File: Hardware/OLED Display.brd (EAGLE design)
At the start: 50 x 15 mm, 23 parts, among them J1 SM04B-SRSS-TB, J2 SM04B-SRSS-TB, U1 QG-2832TLBFG02, U2 APX803

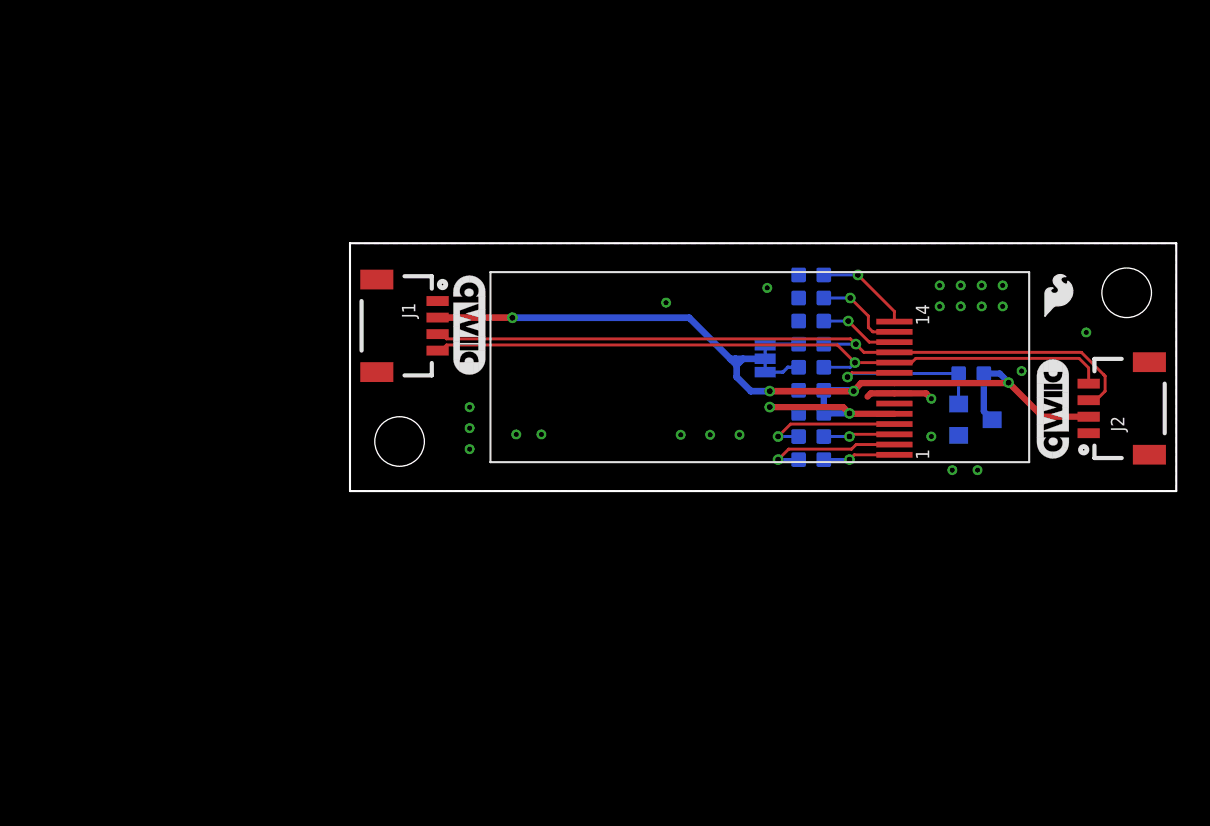
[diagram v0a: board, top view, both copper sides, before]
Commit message: Replaces parts not in the SparkFun Eagle Libraries, adds logos, moves qwiic connectors and standoffs
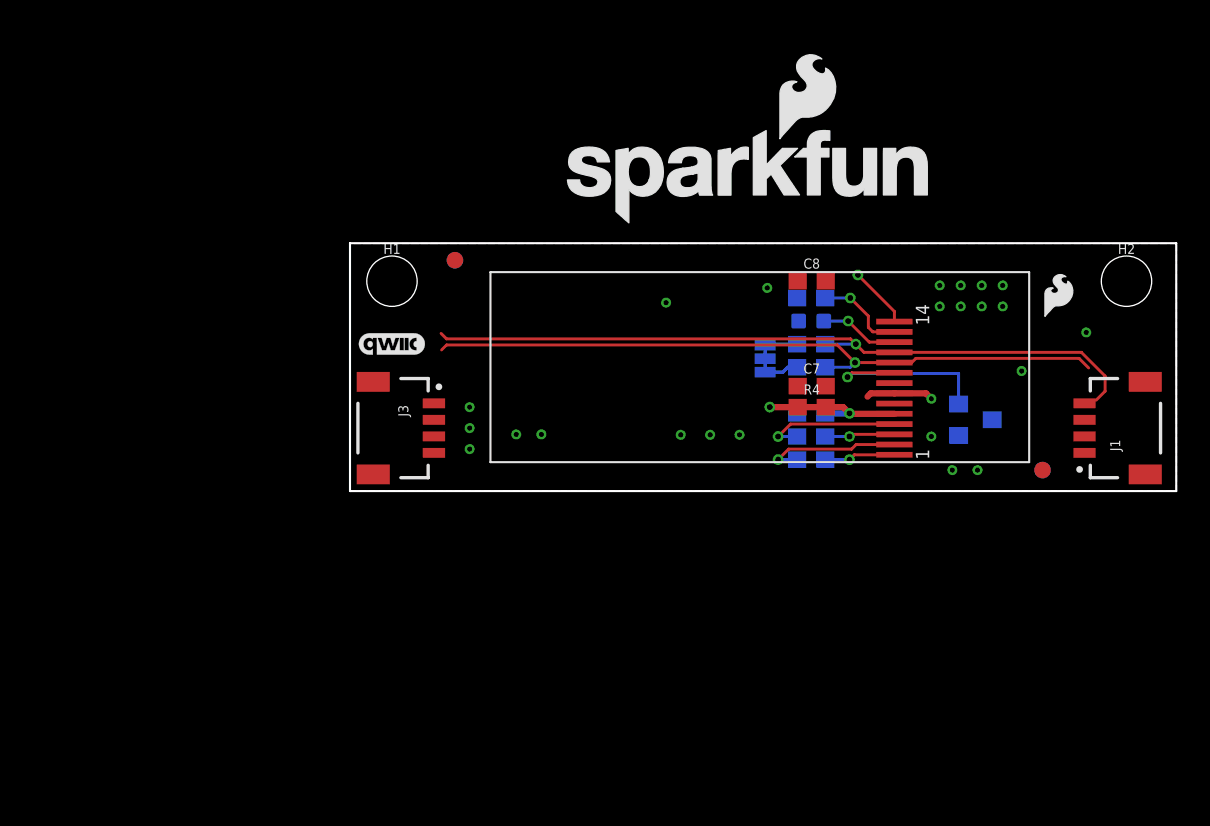
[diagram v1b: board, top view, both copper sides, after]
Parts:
- removed C3: 4.7uF ±10% 6.3V, Discrete:0603
- removed C6: 4.7uF ±10% 16V, Discrete:0603
- removed J2: SM04B-SRSS-TB, Connector:JST-SH-4P
- removed U$11, U$12: (no value), SparkFun-Aesthetics_Font_Logo:QWIIC_6MM
- removed U$6: (no value), Z_silkscreen_package:QWIIC-LOGO-MEDIUM
- added C7, C8: 4.7uF, SparkFun-Capacitors:0603
- added FD1, FD2, FD3, FD4: FIDUCIAL1X2, SparkFun-Aesthetics:FIDUCIAL-1X2
- added FRAME2: FRAME-LETTER, SparkFun-Aesthetics:CREATIVE_COMMONS
- added H1, H2: STAND-OFFTIGHT, SparkFun-Hardware:STAND-OFF-TIGHT
- added J3: QWIIC_RIGHT_ANGLE, SparkFun-Connectors:JST04_1MM_RA
- added LOGO1: SFE_LOGO_NAME_FLAME.2_INCH, SparkFun-Aesthetics:SFE_LOGO_NAME_FLAME_.2
- added LOGO3: QWIIC_LOGO_4MM, SparkFun-Aesthetics:QWIIC_4MM
- added LOGO4: SPECIAL_INSTRUCTIONS-ORDERING, SparkFun-Aesthetics:ORDERING_INSTRUCTIONS
- C1, C2: value 1uF ±10% 16V -> 1.0uF; device Discrete:0603 -> SparkFun-Capacitors:0603
- C4: value 0.1uF ±10% 25V -> 0.1uF; device Discrete:0603 -> SparkFun-Capacitors:0603
- C5: value 2.2uF ±10% 16V -> 2.2uF; device Discrete:0603 -> SparkFun-Capacitors:0603
- J1: value SM04B-SRSS-TB -> QWIIC_RIGHT_ANGLE; device Connector:JST-SH-4P -> SparkFun-Connectors:JST04_1MM_RA
- R1, R2, R4: value 10K ±5% -> 10k; device Discrete:0603 -> SparkFun-Resistors:0603
- moved J1 39.6 mm to (44.5, 3.81)
- moved R4 9.86 mm to (27.9, 5.08), flipped to the top, turned to 0 degrees
- renumbered JP1 to I2C
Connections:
- net OLED_RST# renamed RST
- removed net +3V3: C3.1, C4.1, I2C.2, J1.2, J2.2, R4.2, U1.5, U1.8, U2.3
- new net 3.3V: C4.1, C8.2, I2C.2, J1.2, J3.2, R4.2, U1.5, U1.8, U2.3
- net GND: now also C7.1, C8.1, J3.1; no longer C3.2, C6.2, J1.NC1, J1.NC2, J2.1, J2.NC1, J2.NC2
- net N$7: now also C7.2; no longer C6.1
- net SCL: now also J3.4; no longer J2.4
- net SDA: now also J3.3; no longer J2.3
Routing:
- net +3V3: track 63.0 -> 0.00 mm, vias 6 -> 0
- net 3.3V: track 0.00 -> 9.18 mm, vias 0 -> 2
- net N$7: track 5.81 -> 3.74 mm
- net SCL: track 43.3 -> 42.0 mm
- net SDA: track 45.5 -> 44.8 mm

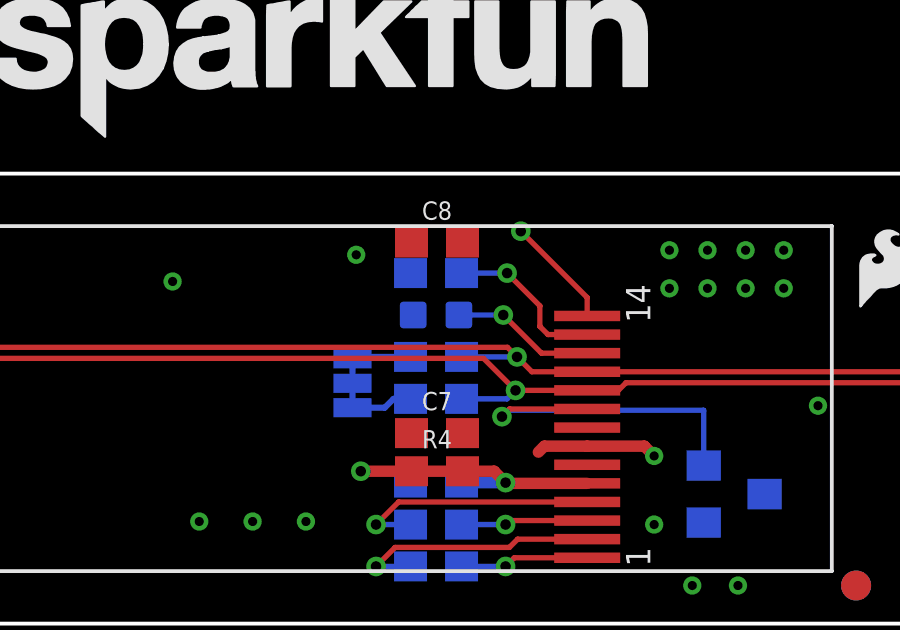
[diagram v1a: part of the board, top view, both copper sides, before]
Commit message: Replaces more parts
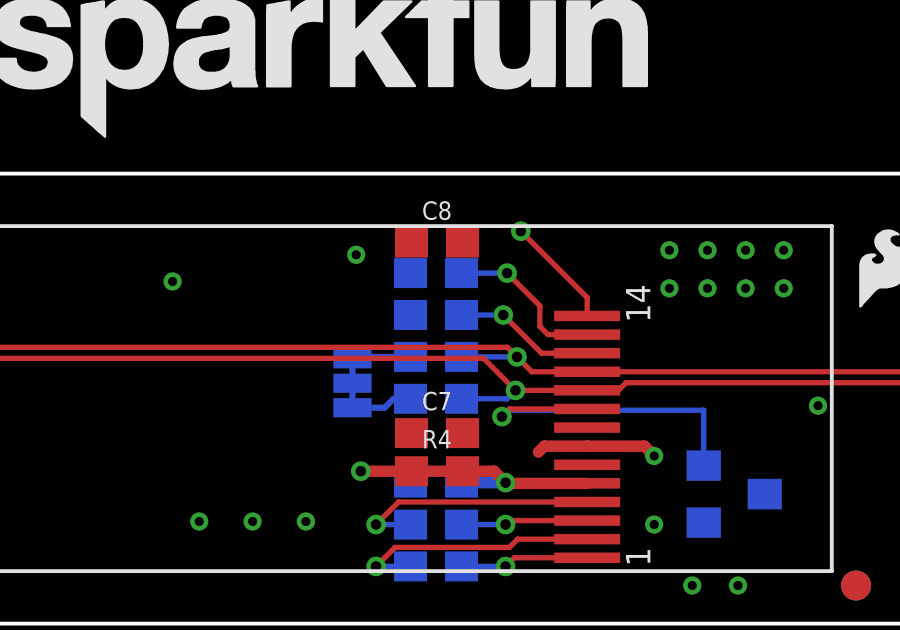
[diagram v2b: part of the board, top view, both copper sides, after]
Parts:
- R3: value 560K 10% -> 470k; device Discrete:0603 -> SparkFun-Resistors:0603
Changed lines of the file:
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@@
 <attribute name="VALUE" value="10k" x="29.305" y="7.4549" size="0.635" layer="28" ratio="10" rot="MR0"/>
 </element>
-<element name="R3" library="Discrete" package="0603" value="560K 10%" x="27.908" y="10.287" smashed="yes" rot="MR180">
+<element name="R3" library="SparkFun-Resistors" package="0603" value="470k" x="27.908" y="10.287" smashed="yes" rot="MR180">
 <attribute name="NAME" x="27.273" y="10.668" size="0.8128" layer="26" ratio="10" rot="MR180"/>
 <attribute name="NAME" x="26.638" y="10.541" size="0.635" layer="34" ratio="10" rot="MR180"/>
-<attribute name="VALUE" x="26.511" y="11.7221" size="0.635" layer="28" ratio="10" rot="MR180"/>
+<attribute name="PROD_ID" value="RES-16181" x="27.908" y="10.287" size="1.778" layer="28" rot="MR180" display="off"/>
+<attribute name="VALUE" value="470k" x="26.511" y="11.7221" size="0.635" layer="28" ratio="10" rot="MR180"/>
 </element>
 <element name="U1" library="Module" package="OLED-12832" value="QG-2832TLBFG02" x="8.5" y="1.75" smashed="yes"/>
@@
 <wire x1="31.4218" y1="9.015" x2="30.1498" y2="10.287" width="0.1778" layer="1"/>
 <via x="30.1498" y="10.287" extent="1-16" drill="0.35"/>
-<wire x1="28.67" y1="10.287" x2="30.1498" y2="10.287" width="0.1778" layer="16"/>
+<wire x1="28.758" y1="10.287" x2="30.1498" y2="10.287" width="0.1778" layer="16"/>
 </signal>
 <signal name="GND">
-<contactref element="U1" pad="7"/>
 <polygon width="0.1778" layer="1">
 <vertex x="0" y="0"/>
@@
 <vertex x="0" y="14.986"/>
 </polygon>
-<via x="35.179" y="5.588" extent="1-16" drill="0.3048"/>
-<wire x1="32.945" y1="5.915" x2="34.852" y2="5.915" width="0.381" layer="1"/>
-<wire x1="34.852" y1="5.915" x2="35.179" y2="5.588" width="0.381" layer="1"/>
-<wire x1="32.945" y1="5.915" x2="31.5182" y2="5.915" width="0.381" layer="1"/>
-<wire x1="31.5182" y1="5.915" x2="31.3182" y2="5.715" width="0.381" layer="1"/>
 <via x="35.179" y="3.302" extent="1-16" drill="0.3048"/>
 <via x="40.64" y="7.2644" extent="1-16" drill="0.3048"/>
@@
 <contactref element="J3" pad="1"/>
 <contactref element="U2" pad="1"/>
-<wire x1="5.08" y1="5.31" x2="44.45" y2="2.31" width="0" layer="19" extent="1-1"/>
-<wire x1="27.09" y1="12.7" x2="5.08" y2="5.31" width="0" layer="19" extent="1-1"/>
-<wire x1="27.09" y1="6.35" x2="27.09" y2="12.7" width="0" layer="19" extent="1-1"/>
-<wire x1="7.239" y1="2.54" x2="27.09" y2="6.35" width="0" layer="19" extent="1-1"/>
-<wire x1="7.239" y1="3.81" x2="7.239" y2="2.54" width="0" layer="19" extent="1-1"/>
-<wire x1="7.239" y1="5.08" x2="7.239" y2="3.81" width="0" layer="19" extent="1-1"/>
-<wire x1="10.0584" y1="3.429" x2="7.239" y2="3.81" width="0" layer="19" extent="1-1"/>
-<wire x1="11.5824" y1="3.429" x2="10.0584" y2="3.429" width="0" layer="19" extent="1-1"/>
-<wire x1="20.0152" y1="3.4036" x2="11.5824" y2="3.429" width="0" layer="19" extent="1-1"/>
-<wire x1="21.7932" y1="3.4036" x2="20.0152" y2="3.4036" width="0" layer="19" extent="1-1"/>
-<wire x1="23.5712" y1="3.4036" x2="21.7932" y2="3.4036" width="0" layer="19" extent="1-1"/>
-<wire x1="27.058" y1="4.699" x2="23.5712" y2="3.4036" width="0" layer="19" extent="16-16"/>
-<wire x1="31.3182" y1="5.715" x2="27.058" y2="4.699" width="0" layer="19" extent="1-16"/>
-<wire x1="35.179" y1="3.302" x2="35.179" y2="5.588" width="0" layer="19" extent="1-1"/>
-<wire x1="36.83" y1="3.368" x2="35.179" y2="3.302" width="0" layer="19" extent="16-16"/>
-<wire x1="36.449" y1="1.27" x2="36.83" y2="3.368" width="0" layer="19" extent="16-16"/>
-<wire x1="37.973" y1="1.27" x2="36.449" y2="1.27" width="0" layer="19" extent="1-1"/>
-<wire x1="40.64" y1="7.2644" x2="36.83" y2="3.368" width="0" layer="19" extent="16-16"/>
+<contactref element="U1" pad="7"/>
+<via x="35.179" y="5.588" extent="1-16" drill="0.3048"/>
+<wire x1="32.945" y1="5.915" x2="34.852" y2="5.915" width="0.381" layer="1"/>
+<wire x1="34.852" y1="5.915" x2="35.179" y2="5.588" width="0.381" layer="1"/>
+<wire x1="32.945" y1="5.915" x2="31.5182" y2="5.915" width="0.381" layer="1"/>
+<wire x1="31.5182" y1="5.915" x2="31.3182" y2="5.715" width="0.381" layer="1"/>
+<wire x1="40.64" y1="7.2644" x2="44.5516" y2="9.6012" width="0" layer="19" extent="1-1"/>
 <wire x1="39.497" y1="11.176" x2="40.64" y2="7.2644" width="0" layer="19" extent="1-1"/>
 <wire x1="39.497" y1="12.446" x2="39.497" y2="11.176" width="0" layer="19" extent="1-1"/>
@@
 <wire x1="36.957" y1="11.176" x2="38.227" y2="11.176" width="0" layer="19" extent="1-1"/>
 <wire x1="35.687" y1="11.176" x2="35.687" y2="12.446" width="0" layer="19" extent="1-1"/>
-<wire x1="44.5516" y1="9.6012" x2="40.64" y2="7.2644" width="0" layer="19" extent="1-1"/>
-<wire x1="27.146" y1="10.287" x2="27.058" y2="4.699" width="0" layer="19" extent="16-16"/>
-<wire x1="27.058" y1="11.684" x2="27.146" y2="10.287" width="0" layer="19" extent="16-16"/>
-<wire x1="25.2476" y1="12.2936" x2="27.058" y2="11.684" width="0" layer="19" extent="16-16"/>
+<wire x1="36.83" y1="3.368" x2="40.64" y2="7.2644" width="0" layer="19" extent="16-16"/>
+<wire x1="35.179" y1="3.302" x2="36.83" y2="3.368" width="0" layer="19" extent="16-16"/>
+<wire x1="36.449" y1="1.27" x2="36.83" y2="3.368" width="0" layer="19" extent="16-16"/>
+<wire x1="37.973" y1="1.27" x2="36.449" y2="1.27" width="0" layer="19" extent="1-1"/>
+<wire x1="35.179" y1="5.588" x2="35.179" y2="3.302" width="0" layer="19" extent="1-1"/>
+<wire x1="27.09" y1="6.35" x2="31.3182" y2="5.715" width="0" layer="19" extent="1-1"/>
+<wire x1="27.058" y1="4.699" x2="27.09" y2="6.35" width="0" layer="19" extent="1-16"/>
+<wire x1="23.5712" y1="3.4036" x2="27.058" y2="4.699" width="0" layer="19" extent="16-16"/>
+<wire x1="21.7932" y1="3.4036" x2="23.5712" y2="3.4036" width="0" layer="19" extent="1-1"/>
+<wire x1="20.0152" y1="3.4036" x2="21.7932" y2="3.4036" width="0" layer="19" extent="1-1"/>
+<wire x1="27.058" y1="10.287" x2="27.09" y2="6.35" width="0" layer="19" extent="1-16"/>
+<wire x1="27.058" y1="11.684" x2="27.058" y2="10.287" width="0" layer="19" extent="16-16"/>
+<wire x1="27.09" y1="12.7" x2="27.058" y2="11.684" width="0" layer="19" extent="1-16"/>
+<wire x1="25.2476" y1="12.2936" x2="27.09" y2="12.7" width="0" layer="19" extent="1-1"/>
 <wire x1="19.1262" y1="11.4046" x2="25.2476" y2="12.2936" width="0" layer="19" extent="1-1"/>
+<wire x1="44.45" y1="2.31" x2="40.64" y2="7.2644" width="0" layer="19" extent="1-1"/>
+<wire x1="11.5824" y1="3.429" x2="20.0152" y2="3.4036" width="0" layer="19" extent="1-1"/>
+<wire x1="10.0584" y1="3.429" x2="11.5824" y2="3.429" width="0" layer="19" extent="1-1"/>
+<wire x1="7.239" y1="3.81" x2="10.0584" y2="3.429" width="0" layer="19" extent="1-1"/>
+<wire x1="7.239" y1="5.08" x2="7.239" y2="3.81" width="0" layer="19" extent="1-1"/>
+<wire x1="7.239" y1="2.54" x2="7.239" y2="3.81" width="0" layer="19" extent="1-1"/>
+<wire x1="5.08" y1="5.31" x2="7.239" y2="5.08" width="0" layer="19" extent="1-1"/>
 </signal>
 <signal name="SCL">
